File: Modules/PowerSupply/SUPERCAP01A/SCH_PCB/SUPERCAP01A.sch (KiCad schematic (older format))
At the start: 22 parts, among them J1 JUMP_3X2, J10 JUMP_2x1, J11 JUMP_3X2, J2 CONN1_1, J3 CONN1_1, J4 CONN1_1, J5 CONN1_1, J6 CONN1_1, J7 CONN1_1, J8 CONN1_1, J9 JUMP_2x1, U1 LTC3625

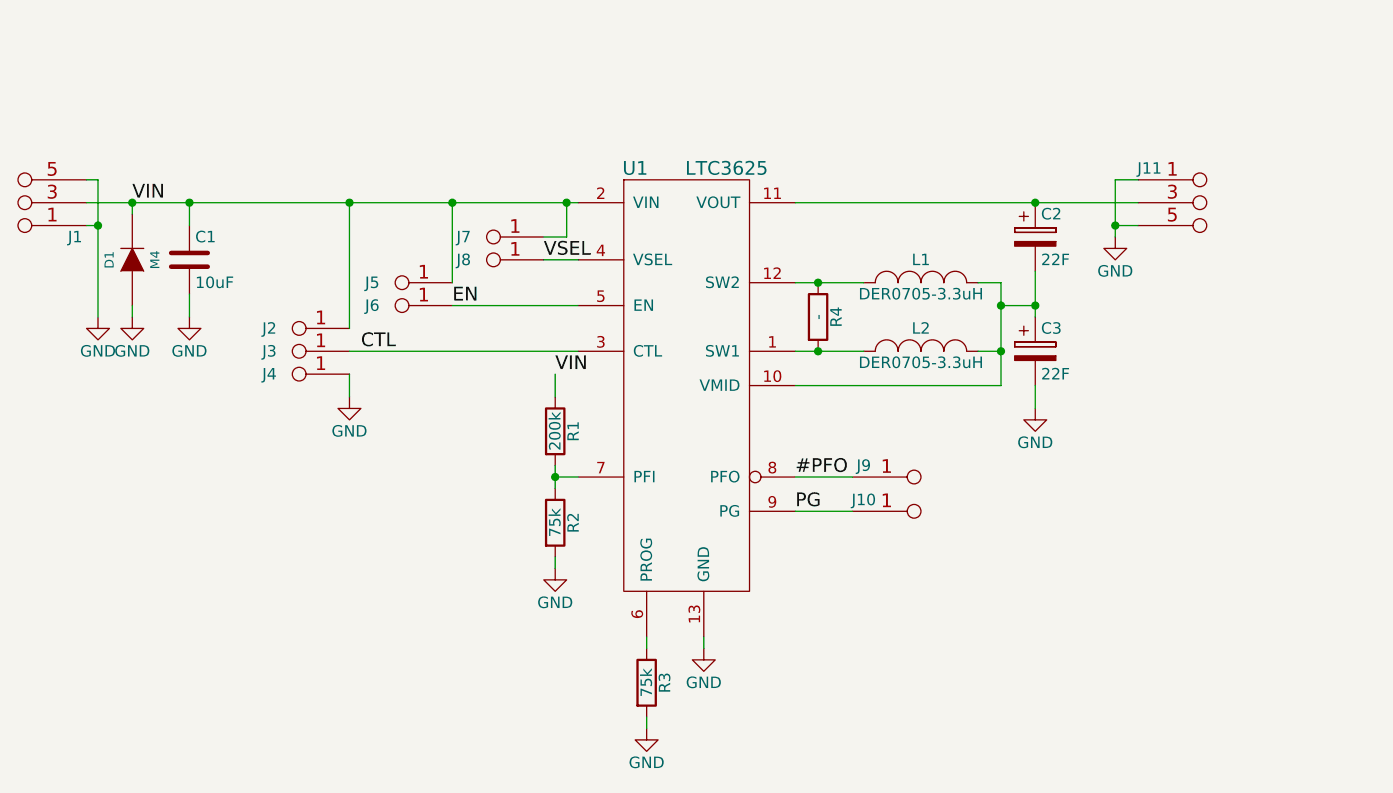
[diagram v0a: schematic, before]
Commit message: 
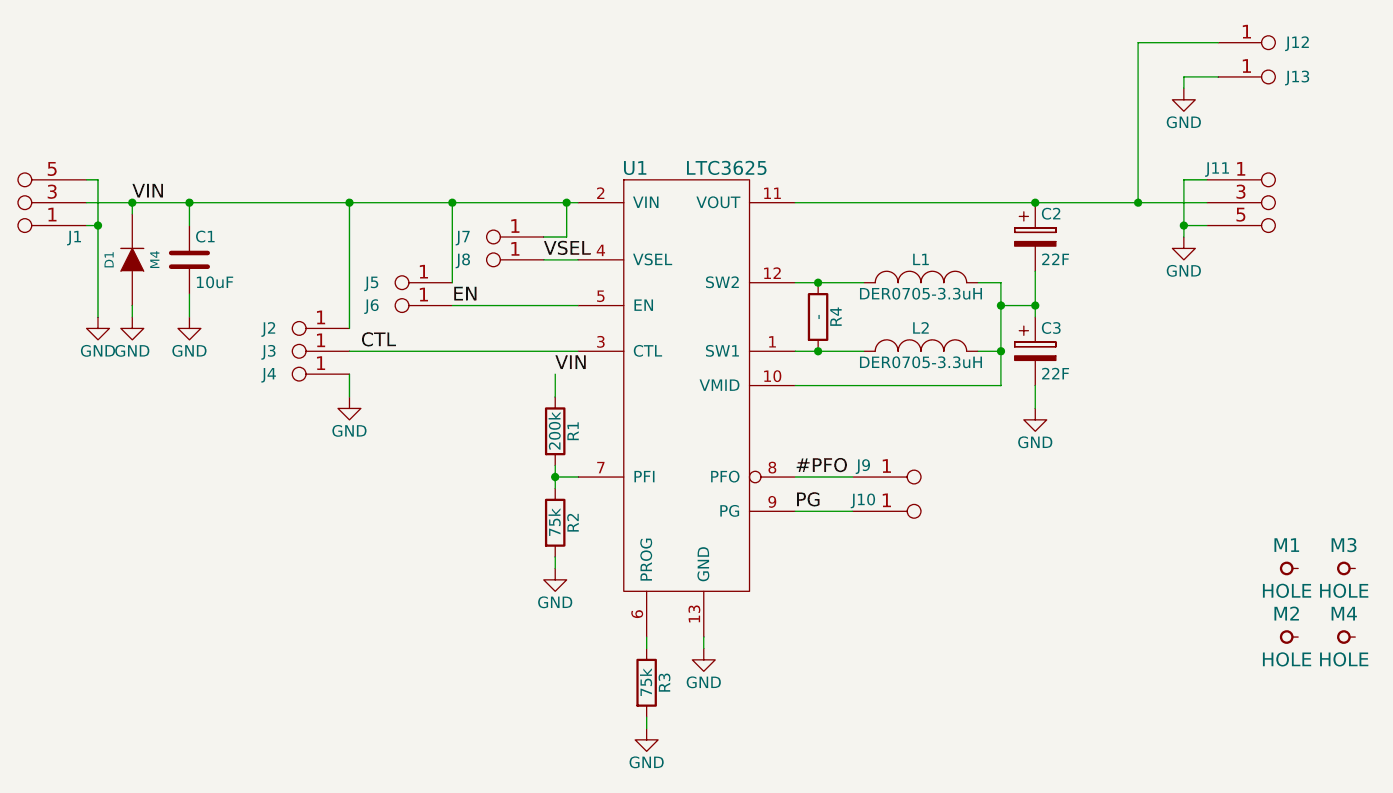
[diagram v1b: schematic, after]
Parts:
- added J12, J13: CONN1_1, Mlab_CON:WAGO256, symbol CONN1_1
- added M1, M2, M3, M4: HOLE, Mlab_Mechanical:MountingHole_3mm, symbol HOLE
- U1: footprint (none) -> Mlab_IO:DFN-12-1EP_3x4mm_Pitch0.5mm
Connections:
- net GND: now also J13.1 (P1)
- net at C2.1, J11.3 (4), J11.4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: now also J12.1 (P1)
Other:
- moved on the sheet: J11
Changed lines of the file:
@@
 LIBS:MLAB_T
 LIBS:MLAB_U
+LIBS:SUPERCAP01A-cache
 EELAYER 25 0
 EELAYER END
@@
 F 0 "U1" H 6200 4250 60  0000 C CNN
 F 1 "LTC3625" H 6600 4250 60  0000 C CNN
-F 2 "" H 6950 2600 60  0001 C CNN
+F 2 "Mlab_IO:DFN-12-1EP_3x4mm_Pitch0.5mm" H 6950 2600 60  0001 C CNN
 F 3 "" H 6950 2600 60  0000 C CNN
 	1    6400 3350
@@
 Wire Wire Line
 	4000 3100 4000 3050
-Wire Wire Line
-	4000 2650 4000 2600
 Connection ~ 4000 2600
 Wire Wire Line
@@
 Connection ~ 7000 3250
 Wire Wire Line
-	6900 2600 8400 2600
-Wire Wire Line
 	7700 2950 7800 2950
 Wire Wire Line
@@
 L JUMP_3X2 J11
 U 1 1 56E8C89C
-P 8800 2650
-F 0 "J11" H 8450 2850 50  0000 C CNN
-F 1 "JUMP_3X2" V 8800 2700 40  0001 C CNN
-F 2 "Mlab_Pin_Headers:Straight_2x03" H 8800 2650 60  0001 C CNN
-F 3 "" H 8800 2650 60  0000 C CNN
-	1    8800 2650
+P 9100 2650
+F 0 "J11" H 8750 2850 50  0000 C CNN
+F 1 "JUMP_3X2" V 9100 2700 40  0001 C CNN
+F 2 "Mlab_Pin_Headers:Straight_2x03" H 9100 2650 60  0001 C CNN
+F 3 "" H 9100 2650 60  0000 C CNN
+	1    9100 2650
 	1    0    0    -1
 $EndComp
@@
 L GND #PWR09
 U 1 1 56E8CF84
-P 8300 2750
-F 0 "#PWR09" H 8300 2500 50  0001 C CNN
-F 1 "GND" H 8300 2600 50  0000 C CNN
-F 2 "" H 8300 2750 50  0000 C CNN
-F 3 "" H 8300 2750 50  0000 C CNN
-	1    8300 2750
-	1    0    0    -1
-$EndComp
-Wire Wire Line
-	8400 2500 8300 2500
-Wire Wire Line
-	8300 2500 8300 2750
-Wire Wire Line
-	8400 2700 8300 2700
-Connection ~ 8300 2700
+P 8600 2750
+F 0 "#PWR09" H 8600 2500 50  0001 C CNN
+F 1 "GND" H 8600 2600 50  0000 C CNN
+F 2 "" H 8600 2750 50  0000 C CNN
+F 3 "" H 8600 2750 50  0000 C CNN
+	1    8600 2750
+	1    0    0    -1
+$EndComp
+Wire Wire Line
+	8700 2500 8600 2500
+Wire Wire Line
+	8600 2500 8600 2750
+Wire Wire Line
+	8700 2700 8600 2700
+Connection ~ 8600 2700
+Wire Wire Line
+	6900 2600 8700 2600
+$Comp
+L HOLE M1
+U 1 1 56EBF2B1
+P 9050 4200
+F 0 "M1" H 9050 4300 60  0000 C CNN
+F 1 "HOLE" H 9050 4100 60  0000 C CNN
+F 2 "Mlab_Mechanical:MountingHole_3mm" H 9050 4200 60  0001 C CNN
+F 3 "" H 9050 4200 60  0000 C CNN
+	1    9050 4200
+	1    0    0    -1
+$EndComp
+$Comp
+L HOLE M3
+U 1 1 56EBF4F9
+P 9300 4200
+F 0 "M3" H 9300 4300 60  0000 C CNN
+F 1 "HOLE" H 9300 4100 60  0000 C CNN
+F 2 "Mlab_Mechanical:MountingHole_3mm" H 9300 4200 60  0001 C CNN
+F 3 "" H 9300 4200 60  0000 C CNN
+	1    9300 4200
+	1    0    0    -1
+$EndComp
+$Comp
+L HOLE M2
+U 1 1 56EBF563
+P 9050 4500
+F 0 "M2" H 9050 4600 60  0000 C CNN
+F 1 "HOLE" H 9050 4400 60  0000 C CNN
+F 2 "Mlab_Mechanical:MountingHole_3mm" H 9050 4500 60  0001 C CNN
+F 3 "" H 9050 4500 60  0000 C CNN
+	1    9050 4500
+	1    0    0    -1
+$EndComp
+$Comp
+L HOLE M4
+U 1 1 56EBF5DC
+P 9300 4500
+F 0 "M4" H 9300 4600 60  0000 C CNN
+F 1 "HOLE" H 9300 4400 60  0000 C CNN
+F 2 "Mlab_Mechanical:MountingHole_3mm" H 9300 4500 60  0001 C CNN
+F 3 "" H 9300 4500 60  0000 C CNN
+	1    9300 4500
+	1    0    0    -1
+$EndComp
+Wire Wire Line
+	4000 2650 4000 2600
+$Comp
+L CONN1_1 J12
+U 1 1 56EBF31C
+P 9050 1950
+F 0 "J12" H 9100 2000 50  0000 C CNN
+F 1 "CONN1_1" H 9150 1900 40  0001 C CNN
+F 2 "Mlab_CON:WAGO256" H 9100 1900 60  0001 C CNN
+F 3 "" H 9100 1900 60  0000 C CNN
+	1    9050 1950
+	1    0    0    -1
+$EndComp
+$Comp
+L CONN1_1 J13
+U 1 1 56EBF84C
+P 9050 2100
+F 0 "J13" H 9100 2150 50  0000 C CNN
+F 1 "CONN1_1" H 9150 2050 40  0001 C CNN
+F 2 "Mlab_CON:WAGO256" H 9100 2050 60  0001 C CNN
+F 3 "" H 9100 2050 60  0000 C CNN
+	1    9050 2100
+	1    0    0    -1
+$EndComp
+$Comp
+L GND #PWR010
+U 1 1 56EBF8B2
+P 8600 2100
+F 0 "#PWR010" H 8600 1850 50  0001 C CNN
+F 1 "GND" H 8600 1950 50  0000 C CNN
+F 2 "" H 8600 2100 50  0000 C CNN
+F 3 "" H 8600 2100 50  0000 C CNN
+	1    8600 2100
+	1    0    0    -1
+$EndComp
+Wire Wire Line
+	8750 2050 8600 2050
+Wire Wire Line
+	8600 2050 8600 2100
+Wire Wire Line
+	8750 1900 8400 1900
+Wire Wire Line
+	8400 1900 8400 2600
+Connection ~ 8400 2600
 $EndSCHEMATC
